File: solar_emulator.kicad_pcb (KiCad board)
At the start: 2 copper layers, 125.5 x 75 mm, 69 parts, among them J1 USB_C_Receptacle_USB2.0_16P, J2 Conn_01x02, J3 Conn_01x02, J4 Conn_01x02, J5 Conn_01x02, J6 Conn_01x03, J7 Conn_01x04, Q1 IRFZ44N, Q2 IRFZ44N, Q3 IRFZ44N, Q4 IRFZ44N, Q5 IRFZ44N, Q6 IRFZ44N, Q7 IRFZ44N, Q8 IRFZ44N, SW1 SW_Push, SW2 SW_Push, U1 ESP32-S3-WROOM-1, U2 LD1117S33TR_SOT223, U3 HIP4081AIPZ, U4 HIP4081AIPZ, U5 LM393, U6 LM393

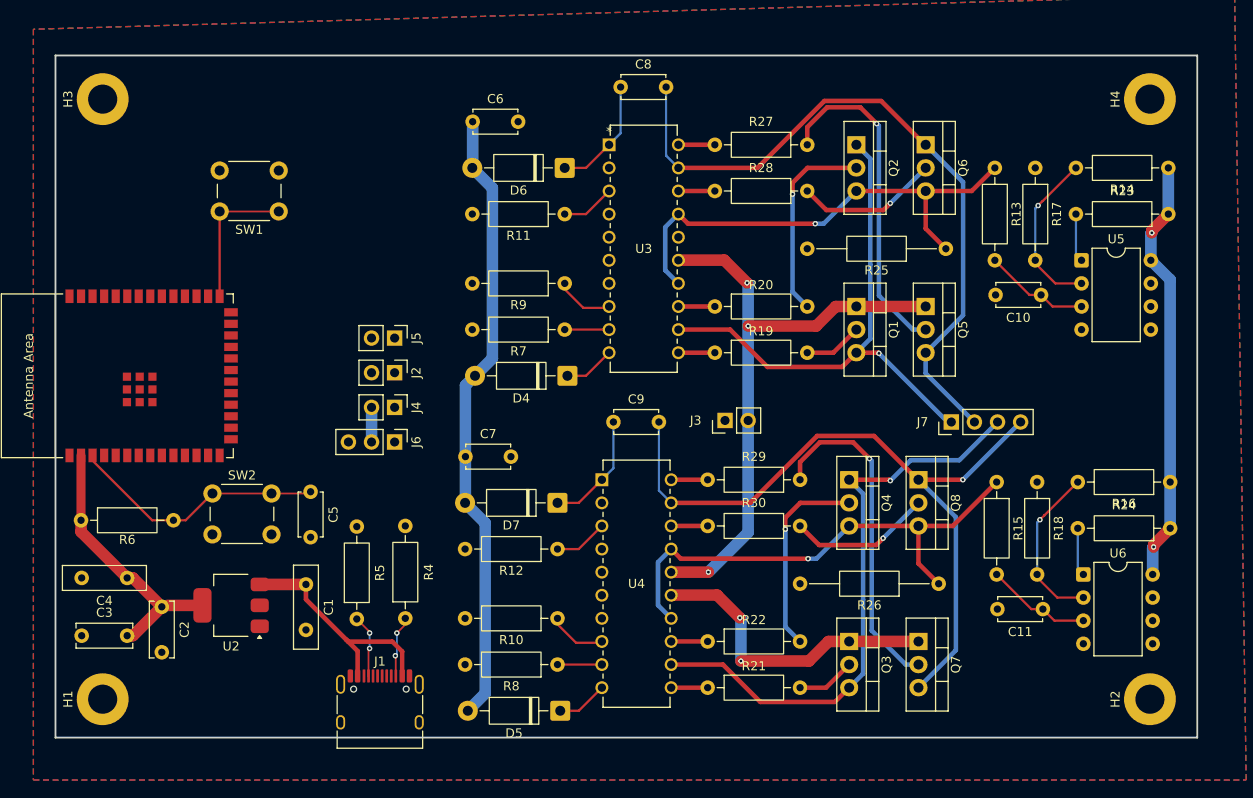
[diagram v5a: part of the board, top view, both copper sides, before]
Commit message: implement +12V copper fills, routing basically complete
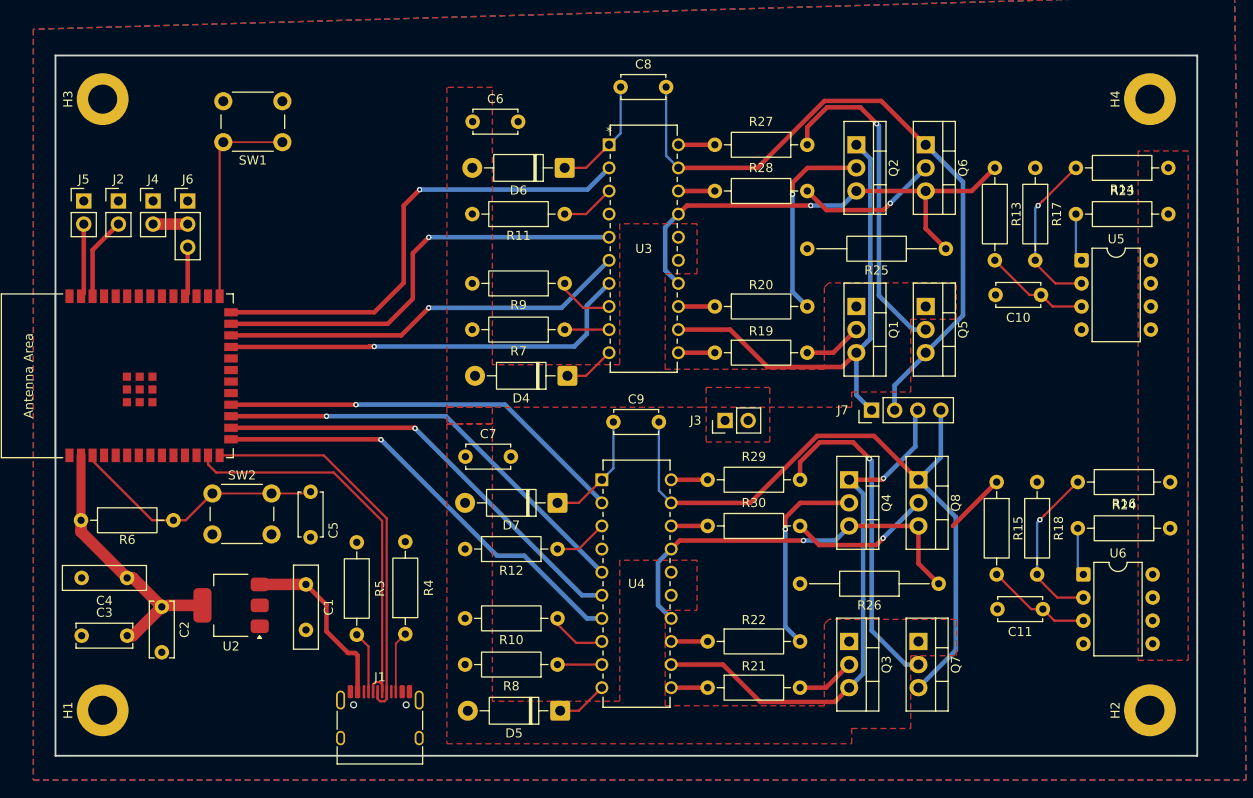
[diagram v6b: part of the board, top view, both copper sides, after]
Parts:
- moved J5 37.4 mm to (118.6, 90.0), turned to 0 degrees
- moved J2 35.8 mm to (122.4, 90.0), turned to 0 degrees
- moved J4 34.9 mm to (126.2, 90.0), turned to 0 degrees
- moved J6 34.9 mm to (130.0, 90.0), turned to 0 degrees
- moved J7 8.87 mm to (205.2, 113.0)
- moved SW1 7.63 mm to (140.4, 83.5)
- moved R4 1.73 mm to (153.9, 137.6)
- moved J1 1.73 mm to (151.1, 148.0)
- moved R5 1.73 mm to (148.6, 137.7)
- moved H1 1.22 mm to (120.7, 146.0)
- moved H2 1.22 mm to (235.8, 146.0)
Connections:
- U1 pad 12: AHI2 -> unconnected-(U1-GPIO8/TOUCH8/ADC1_CH7/SUBSPICS1-Pad12)
- U1 pad 15: ALI1 -> AHI2
- U1 pad 16: unconnected-(U1-GPIO46-Pad16) -> ALI2
- U1 pad 17: SERVO -> BLI2
- U1 pad 18: LIMIT1 -> BHI2
- U1 pad 19: LIMIT2 -> unconnected-(U1-GPIO11/TOUCH11/ADC2_CH0/FSPID/FSPIIO5/SUBSPID-Pad19)
- U1 pad 23: unconnected-(U1-GPIO21-Pad23) -> AHI1
- U1 pad 24: unconnected-(U1-GPIO47/SPICLK_P/SUBSPICLK_P_DIFF-Pad24) -> ALI1
- U1 pad 25: unconnected-(U1-GPIO48/SPICLK_N/SUBSPICLK_N_DIFF-Pad25) -> BLI1
- U1 pad 26: unconnected-(U1-GPIO45-Pad26) -> BHI1
- U1 pad 30: unconnected-(U1-SPIDQS/GPIO37/FSPIQ/SUBSPIQ-Pad30) -> SERVO
- U1 pad 38: BLI1 -> LIMIT1
- U1 pad 39: BHI1 -> LIMIT2
- U1 pad 4: AHI1 -> unconnected-(U1-GPIO4/TOUCH4/ADC1_CH3-Pad4)
- U1 pad 5: BHI2 -> unconnected-(U1-GPIO5/TOUCH5/ADC1_CH4-Pad5)
- U1 pad 6: BLI2 -> unconnected-(U1-GPIO6/TOUCH6/ADC1_CH5-Pad6)
- U1 pad 7: ALI2 -> unconnected-(U1-GPIO7/TOUCH7/ADC1_CH6-Pad7)
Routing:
- net +12V: track 169.2 -> 0.17 mm, vias 5 -> 0
- net BHI1: track 0.00 -> 53.1 mm, vias 0 -> 1
- net AHI2: track 0.00 -> 48.9 mm, vias 0 -> 1
- net BLI1: track 0.00 -> 48.4 mm, vias 0 -> 1
- net ALI2: track 0.00 -> 48.4 mm, vias 0 -> 1
- net BLI2: track 0.00 -> 47.9 mm, vias 0 -> 1
- net +3V3: track 78.8 -> 31.7 mm, vias 2 -> 0
- net AHI1: track 0.00 -> 46.3 mm, vias 0 -> 1
- net BHI2: track 0.00 -> 45.3 mm, vias 0 -> 1
- net ALI1: track 0.00 -> 45.0 mm, vias 0 -> 1
- net D-: track 0.00 -> 44.3 mm
- net D+: track 0.00 -> 43.1 mm
- net LIMIT1: track 0.00 -> 9.11 mm
- net LIMIT2: track 0.00 -> 8.05 mm
- net GPIO0: track 15.8 -> 23.6 mm
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- added copper zone on F.Cu, net +12V
- added copper zone on F.Cu, net +3V3
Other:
- board size 125.5 x 75 mm -> 125.5 x 77 mm

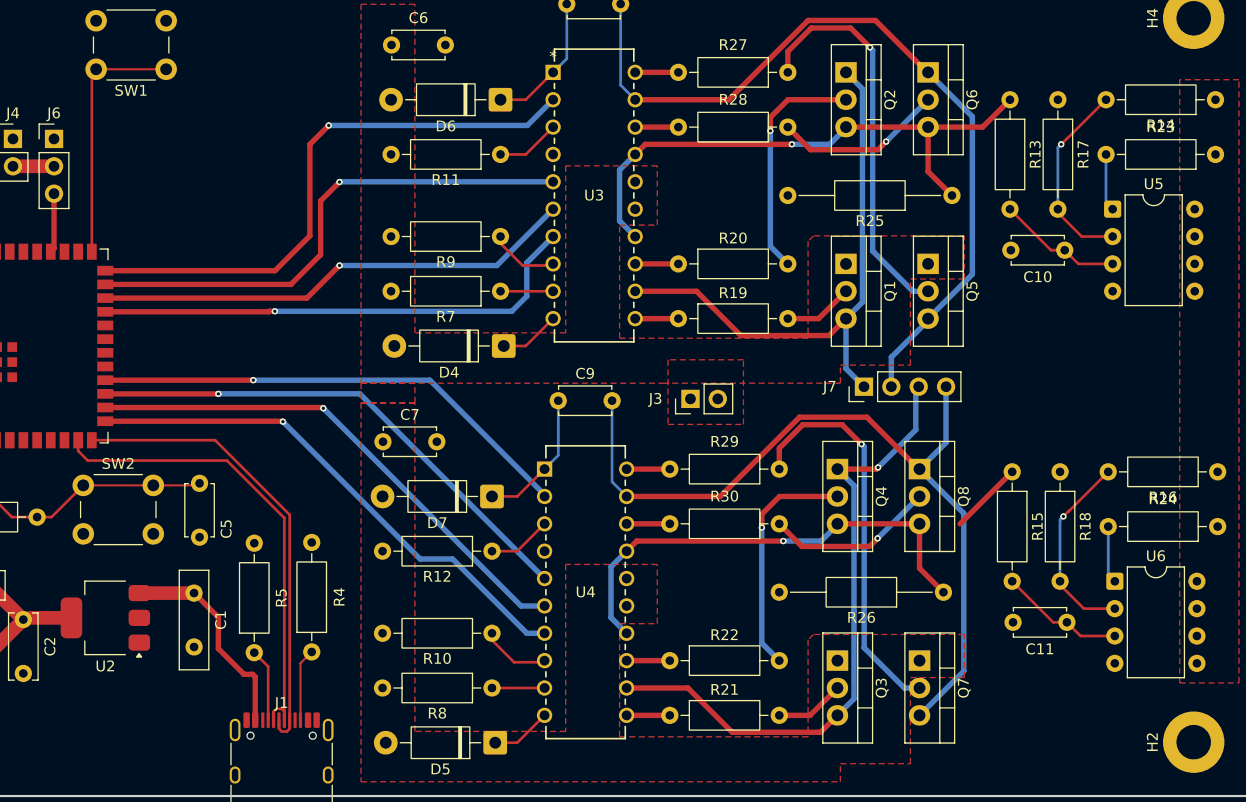
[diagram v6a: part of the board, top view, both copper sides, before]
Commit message: separate 5V servo and +5V usb
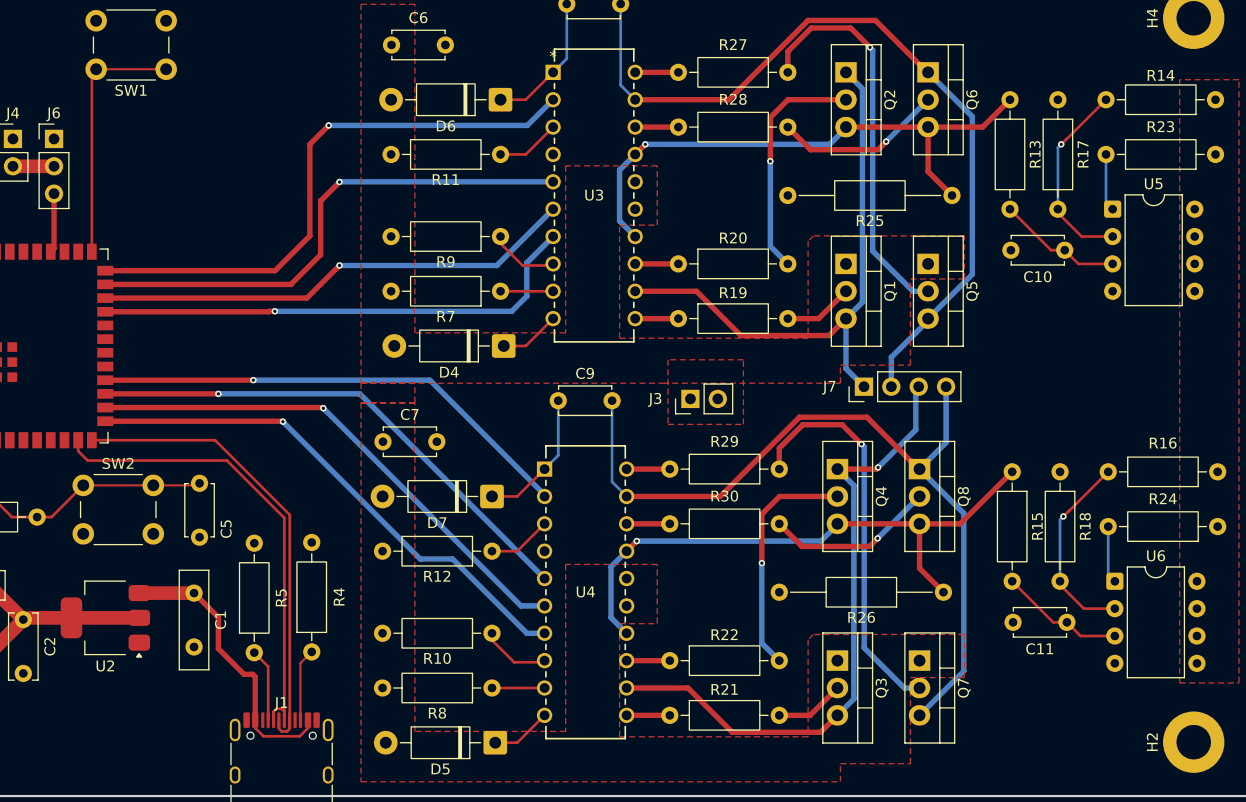
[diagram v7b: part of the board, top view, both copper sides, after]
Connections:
- J4 pad 2: +5V -> 5V
- J6 pad 2: +5V -> 5V
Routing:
- net +3V3: track 31.7 -> 38.0 mm
- net 5V: track 0.00 -> 3.81 mm
- net BLS2: track 51.2 -> 55.0 mm
- net +5V: track 23.7 -> 26.9 mm
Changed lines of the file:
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@@
 		(capping no)
 		(filling no)
-		(zone_defaults)
 		(pcbplotparams
 			(layerselection 0x00000000_00000000_55555555_5755f5ff)
@@
 			(layers "*.Cu" "*.Mask")
 			(remove_unused_layers no)
-			(net "+5V")
+			(net "5V")
 			(pinfunction "Pin_2_2")
 			(pintype "passive")
@@
 		(tags "Resistor Axial_DIN0207 series Axial Horizontal pin pitch 10.16mm 0.25W = 1/4W length 6.3mm diameter 2.5mm")
 		(property "Reference" "R14"
-			(at 5.08 -2.37 0)
+			(at 5.08 2.2225 0)
 			(layer "F.SilkS")
 			(effects
@@
 			(layers "*.Cu" "*.Mask")
 			(remove_unused_layers no)
-			(net "+5V")
+			(net "5V")
 			(pinfunction "Pin_2_2")
 			(pintype "passive")
@@
 		(tags "Resistor Axial_DIN0207 series Axial Horizontal pin pitch 10.16mm 0.25W = 1/4W length 6.3mm diameter 2.5mm")
 		(property "Reference" "R16"
-			(at 5.08 -2.37 0)
+			(at 5.08 2.63525 0)
 			(layer "F.SilkS")
 			(effects
@@
 	)
 	(segment
-		(start 198.5 90.5)
-		(end 184.89 90.5)
-		(width 0.5)
-		(layer "F.Cu")
-		(net "BLS1")
-	)
-	(segment
 		(start 216.205 88.9)
 		(end 218.745 86.36)
@@
 	)
 	(via
-		(at 198.5 90.5)
+		(at 184.89 90.5)
 		(size 0.6)
 		(drill 0.3)
@@
 	)
 	(segment
-		(start 183.95 91.44)
-		(end 182.5 92.89)
+		(start 202 90.5)
+		(end 184.89 90.5)
 		(width 0.5)
 		(layer "B.Cu")
@@
 	)
 	(segment
-		(start 202 90.5)
-		(end 203.52 88.98)
+		(start 183.95 91.44)
+		(end 182.5 92.89)
 		(width 0.5)
 		(layer "B.Cu")
@@
 	)
 	(segment
-		(start 198.5 90.5)
-		(end 202 90.5)
+		(start 203.52 88.9)
+		(end 203.52 88.98)
 		(width 0.5)
 		(layer "B.Cu")
@@
 	(segment
 		(start 203.52 88.98)
-		(end 203.52 88.9)
+		(end 202 90.5)
 		(width 0.5)
 		(layer "B.Cu")
@@
 	)
 	(segment
-		(start 197.7075 127.33)
-		(end 184.0975 127.33)
-		(width 0.5)
-		(layer "F.Cu")
-		(net "BLS2")
-	)
-	(segment
 		(start 210.3475 125.73)
 		(end 210.3475 129.86)
@@
 		(net "BLS2")
 	)
+	(segment
+		(start 210.3475 125.73)
+		(end 214.122 125.73)
+		(width 0.5)
+		(layer "F.Cu")
+		(net "BLS2")
+	)
 	(via
-		(at 197.7075 127.33)
+		(at 184.0975 127.33)
 		(size 0.6)
 		(drill 0.3)
@@
 	)
 	(segment
-		(start 201.2075 127.33)
-		(end 202.7275 125.81)
+		(start 202.7275 125.81)
+		(end 201.2075 127.33)
 		(width 0.5)
 		(layer "B.Cu")
@@
 	)
 	(segment
-		(start 197.7075 127.33)
-		(end 201.2075 127.33)
+		(start 202.7275 125.73)
+		(end 202.7275 125.81)
 		(width 0.5)
 		(layer "B.Cu")
@@
 	)
 	(segment
-		(start 202.7275 125.81)
-		(end 202.7275 125.73)
+		(start 201.2075 127.33)
+		(end 184.0975 127.33)
 		(width 0.5)
 		(layer "B.Cu")
@@
 	)
 	(segment
+		(start 131.62 134.46)
+		(end 137.92 134.46)
+		(width 1.27)
+		(layer "F.Cu")
+		(net "+3V3")
+	)
+	(segment
 		(start 126.515 134.62)
 		(end 127.15 134.62)
@@
 	)
 	(segment
+		(start 152.804999 145.455)
+		(end 153.58 144.679999)
+		(width 0.25)
+		(layer "F.Cu")
+		(net "+5V")
+	)
+	(segment
+		(start 153.58 144.679999)
+		(end 153.58 143.955)
+		(width 0.25)
+		(layer "F.Cu")
+		(net "+5V")
+	)
+	(segment
 		(start 147.6375 139.7)
 		(end 145.25625 137.31875)
@@
 	)
 	(segment
+		(start 149.455001 145.455)
+		(end 152.804999 145.455)
+		(width 0.25)
+		(layer "F.Cu")
+		(net "+5V")
+	)
+	(segment
 		(start 148.43125 139.7)
 		(end 147.6375 139.7)
@@
 	)
 	(segment
-		(start 126.19 92.54)
-		(end 130 92.54)
-		(width 1.27)
+		(start 148.68 144.679999)
+		(end 149.455001 145.455)
+		(width 0.25)
 		(layer "F.Cu")
 		(net "+5V")
@@
 	)
 	(segment
+		(start 148.68 143.955)
+		(end 148.68 144.679999)
+		(width 0.25)
+		(layer "F.Cu")
+		(net "+5V")
+	)
+	(segment
 		(start 207.25 90.25)
 		(end 206.5 91)
@@
 	)
 	(segment
-		(start 197.3475 123.19)
-		(end 202.7275 123.19)
+		(start 195.7075 129.38125)
+		(end 195.7075 124.83)
 		(width 0.5)
 		(layer "F.Cu")
@@
 	)
 	(segment
-		(start 195.7075 126.08)
-		(end 195.7075 124.83)
+		(start 197.3475 123.19)
+		(end 202.7275 123.19)
 		(width 0.5)
 		(layer "F.Cu")
@@
 	)
 	(via
-		(at 195.7075 126.08)
+		(at 195.7075 129.38125)
 		(size 0.6)
 		(drill 0.3)
@@
 	)
 	(segment
-		(start 197.3275 138.43)
+		(start 195.7075 129.38125)
 		(end 195.7075 136.81)
 		(width 0.5)
@@
 	(segment
 		(start 195.7075 136.81)
-		(end 195.7075 126.08)
+		(end 197.3275 138.43)
 		(width 0.5)
 		(layer "B.Cu")
@@
 	)
 	(segment
-		(start 196.5 89.25)
-		(end 196.5 88)
+		(start 196.5 88)
+		(end 198.14 86.36)
 		(width 0.5)
 		(layer "F.Cu")
@@
 	)
 	(segment
-		(start 196.5 88)
-		(end 198.14 86.36)
+		(start 196.5 92.075)
+		(end 196.5 88)
 		(width 0.5)
 		(layer "F.Cu")
@@
 	)
 	(via
-		(at 196.5 89.25)
+		(at 196.5 92.075)
 		(size 0.6)
 		(drill 0.3)
@@
 	)
 	(segment
-		(start 198.12 101.6)
-		(end 196.5 99.98)
+		(start 196.5 99.98)
+		(end 198.12 101.6)
 		(width 0.5)
 		(layer "B.Cu")
@@
 	)
 	(segment
-		(start 196.5 99.98)
-		(end 196.5 89.25)
+		(start 196.5 92.075)
+		(end 196.5 99.98)
 		(width 0.5)
 		(layer "B.Cu")
@@
 	)
 	(segment
+		(start 133.51 100.47)
+		(end 133.51 83.93)
+		(width 0.25)
+		(layer "F.Cu")
+		(net "GPIO0")
+	)
+	(segment
+		(start 140.81 83.53)
+		(end 134.31 83.53)
+		(width 0.2)
+		(layer "F.Cu")
+		(net "GPIO0")
+	)
+	(segment
+		(start 133.51 83.93)
+		(end 133.91 83.53)
+		(width 0.25)
+		(layer "F.Cu")
+		(net "GPIO0")
+	)
+	(segment
 		(start 130 100.17)
 		(end 129.7 100.47)
@@
 	)
 	(segment
-		(start 133.51 100.47)
-		(end 133.51 83.93)
-		(width 0.25)
-		(layer "F.Cu")
-		(net "GPIO0")
-	)
-	(segment
-		(start 140.81 83.53)
-		(end 134.31 83.53)
-		(width 0.2)
-		(layer "F.Cu")
-		(net "GPIO0")
-	)
-	(segment
-		(start 133.51 83.93)
-		(end 133.91 83.53)
-		(width 0.25)
+		(start 126.19 92.54)
+		(end 130 92.54)
+		(width 1.27)
 		(layer "F.Cu")
-		(net "GPIO0")
+		(net "5V")
 	)
 	(zone
